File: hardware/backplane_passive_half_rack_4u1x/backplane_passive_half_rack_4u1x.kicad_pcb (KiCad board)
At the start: 4 copper layers, 141.5 x 128.5 mm, 33 parts

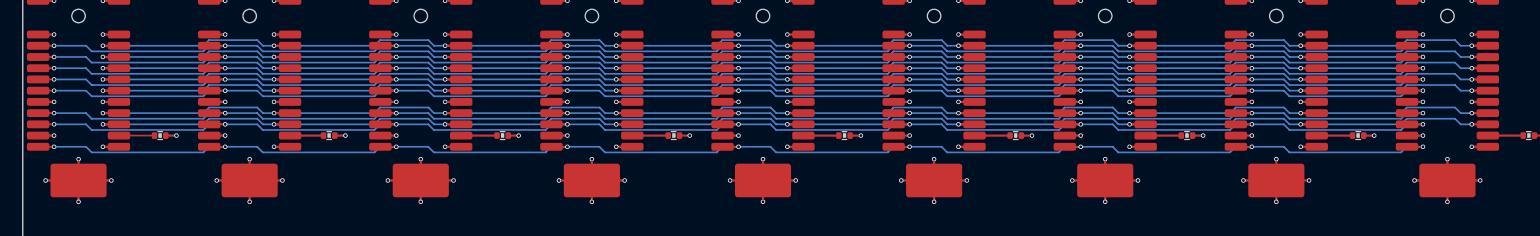
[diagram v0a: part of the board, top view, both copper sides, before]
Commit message: Updated the RAddr values. Made USB a diff pair.
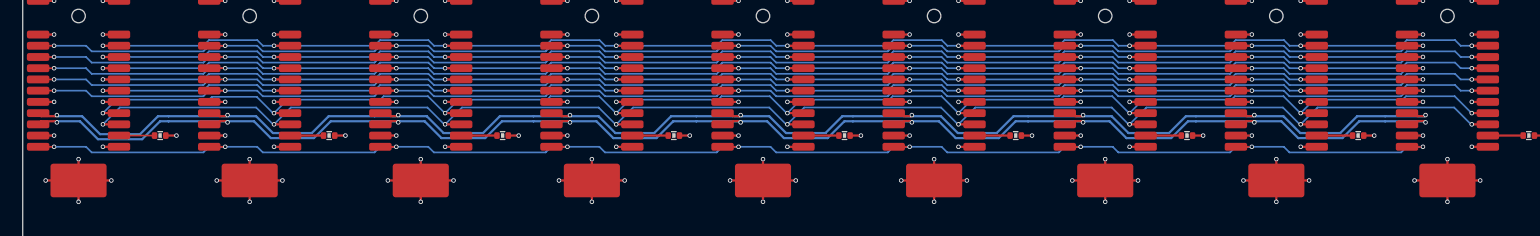
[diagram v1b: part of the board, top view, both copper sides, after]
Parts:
- R10: value 4k09 -> 4k22
- R9: value 3k55 -> 3k65
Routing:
- net /D_N: track 138.0 -> 148.7 mm
- net /D_P: track 138.0 -> 148.7 mm
- net /MGMT_SDA: track 138.1 -> 144.7 mm
- net /MGMT_SCL: track 138.1 -> 144.7 mm

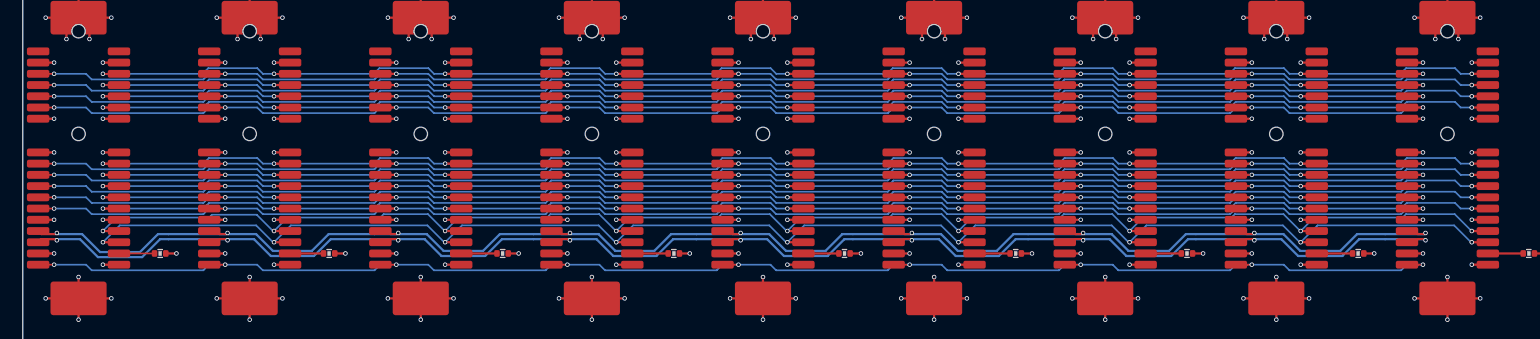
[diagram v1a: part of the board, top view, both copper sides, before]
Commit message: Filleted the tracks.
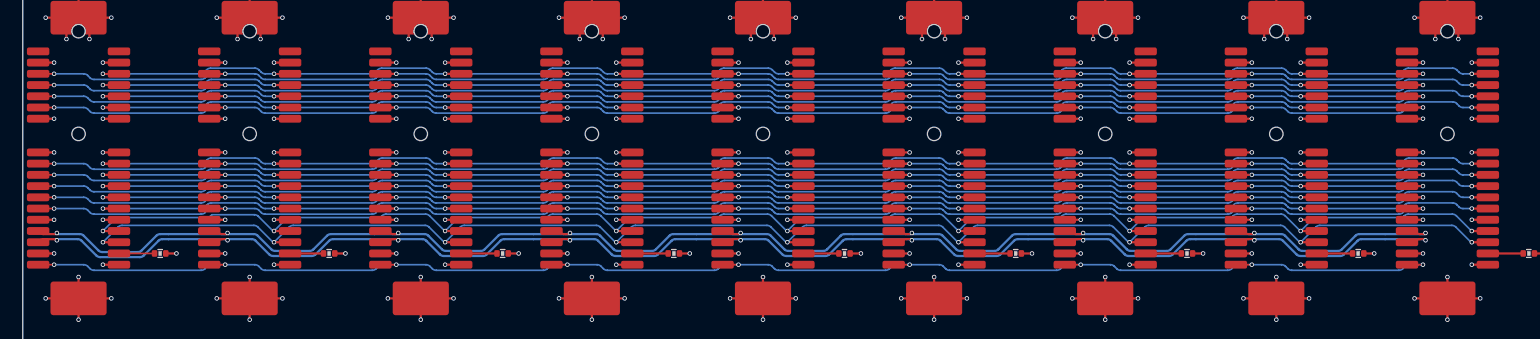
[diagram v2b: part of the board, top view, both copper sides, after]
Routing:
- net /D_P: track 148.7 -> 147.7 mm
- net /D_N: track 148.7 -> 147.7 mm
- net /SLOT1/GPIO4: track 138.0 -> 137.2 mm
- net /JTDO: track 138.1 -> 137.3 mm
- net /JTDI: track 138.1 -> 137.3 mm
- net /VTREF: track 138.0 -> 137.2 mm
- net /SLOT1/TRACE.D3: track 138.0 -> 137.2 mm
- net /SLOT1/TRACE.D2: track 138.0 -> 137.2 mm
- net /SLOT1/GPIO7: track 138.0 -> 137.2 mm
- net /SLOT1/GPIO6: track 138.0 -> 137.2 mm
- net /SLOT1/GPIO5: track 138.0 -> 137.2 mm
- net /SLOT1/GPIO3: track 138.1 -> 137.3 mm
- net /SLOT1/GPIO2: track 138.1 -> 137.3 mm
- net /NRST: track 138.1 -> 137.3 mm
- net /SLOT1/TRACE.D1: track 138.0 -> 137.2 mm
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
